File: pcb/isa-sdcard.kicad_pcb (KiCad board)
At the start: 2 copper layers, 151.6 x 82.7 mm, 41 parts, among them J1 SDCARD, J2 Bus_ISA_8bit_AB_Rev0, SW1 ADDR SEL, U1 74HC00, U10 74HC74, U11 74HC08, U12 74HC04, U2 74HCT32, U3 74HCT139, U4 74HC163, U5 74HC00, U6 74HC165, U7 74HC595, U8 74HCT688, U9 74HCT245, X1 16MHz

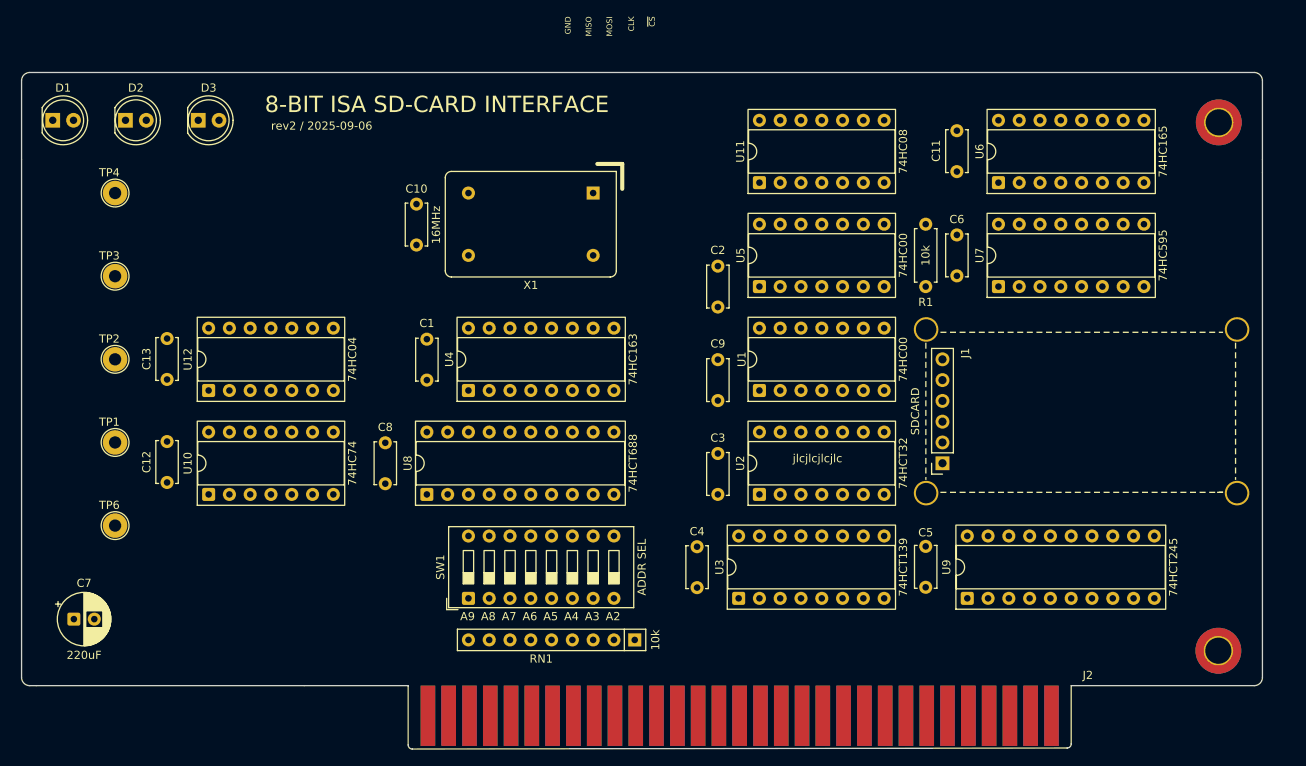
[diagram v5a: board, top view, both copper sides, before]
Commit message: Adding immediate pulse after rwrite and optional pulse after read
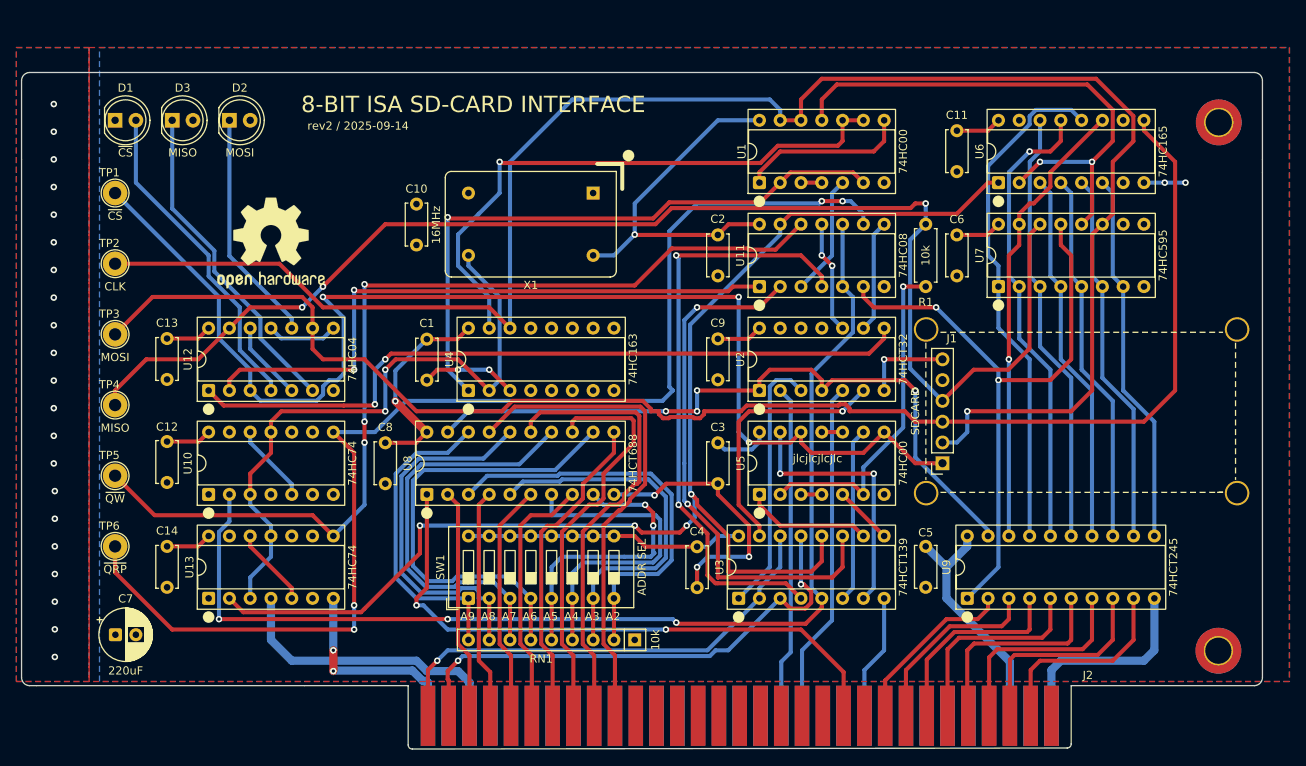
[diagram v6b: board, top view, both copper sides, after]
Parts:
- added C14: 0.1uF, Capacitor_THT:C_Disc_D5.0mm_W2.5mm_P5.00mm, F.Cu at (47.2, 100.5)
- added REF**: OSHW-Logo2_14.6x12mm_SilkScreen, Symbol:OSHW-Logo2_14.6x12mm_SilkScreen, F.Cu at (59.9, 58.4)
- added TP5: ~{QW}, TestPoint:TestPoint_Loop_D2.54mm_Drill1.5mm_Beaded, F.Cu at (40.9, 86.9)
- added U13: 74HC74, Package_DIP:DIP-14_W7.62mm_Socket, F.Cu at (52.3, 101.8)
- D1: value LED -> ~{CS}
- D2: value LED -> MOSI
- D3: value LED -> MISO
- TP6: value ~{Q} -> ~{QRP}
- moved TP1 30.5 mm to (40.9, 52.3)
- moved TP4 25.9 mm to (40.9, 78.2)
- moved U1 25.4 mm to (119.6, 51.0)
- moved U5 25.4 mm to (119.6, 89.1)
- moved U11 12.7 mm to (119.6, 63.7)
- moved U2 12.7 mm to (119.6, 76.4)
- moved D2 12.7 mm to (54.8, 43.4)
- moved TP2 11.7 mm to (40.9, 60.9)
- moved D1 7.62 mm to (40.9, 43.4)
- moved TP3 7.11 mm to (40.9, 69.6)
- moved C7 5.43 mm to (40.9, 106.3)
- moved C11 5.00 mm to (143.7, 49.7), turned to 90 degrees
- moved C2 3.81 mm to (114.5, 62.4)
- moved D3 3.18 mm to (47.9, 43.4)
- moved C9 2.54 mm to (114.5, 75.1)
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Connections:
- U11 pad 1: ~{PULSE} -> Net-(U11-Pad1)
- U11 pad 11: unconnected-(U11-Pad11) -> Net-(U11-Pad11)
- U11 pad 12: GND -> Net-(U13B-~{Q})
- U11 pad 13: GND -> ~{SER_WR}
- U11 pad 2: Net-(U11-Pad2) -> ~{PULSE}
- U12 pad 1: Net-(U11-Pad8) -> Net-(U12-Pad1)
- U12 pad 2: Net-(U11-Pad2) -> Net-(U11-Pad1)
- U2 pad 10: GND -> Net-(U11-Pad11)
- U2 pad 8: unconnected-(U2-Pad8) -> Net-(U12-Pad1)
- U2 pad 9: GND -> Net-(U11-Pad8)
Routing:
- net CLK: track 0.00 -> 216.5 mm, vias 0 -> 1
- net VCC: track 0.00 -> 211.4 mm, vias 0 -> 2
- net MOSI: track 0.00 -> 180.3 mm
- net MISO: track 0.00 -> 165.9 mm, vias 0 -> 3
- net ~{SER_WR}: track 0.00 -> 160.8 mm, vias 0 -> 4
- net ~{CS}: track 0.00 -> 153.0 mm, vias 0 -> 3
- net Net-(U10B-~{Q}): track 0.00 -> 150.8 mm, vias 0 -> 4
- net ~{SER_RD_AND_PULSE}: track 0.00 -> 140.5 mm, vias 0 -> 3
- net GND: track 0.00 -> 127.4 mm, vias 0 -> 31
- net Net-(U13B-~{Q}): track 0.00 -> 118.7 mm, vias 0 -> 3
- net Net-(U12-Pad1): track 0.00 -> 90.5 mm, vias 0 -> 2
- net ~{PORTSEL}: track 0.00 -> 86.8 mm, vias 0 -> 4
- net ~{SER_RD}: track 0.00 -> 78.0 mm, vias 0 -> 2
- net 16MHz: track 0.00 -> 77.7 mm, vias 0 -> 2
- net Net-(U11-Pad1): track 0.00 -> 76.6 mm, vias 0 -> 2
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- added copper zone on B.Cu, net GND
- added copper zone on F.Cu, net GND
- added copper zone on B.Cu, net VCC
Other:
- board text added: "rev2 / 2025-09-14"
- board text removed: "CLK"
- board text removed: "GND"
- board text removed: "MISO"
- board text removed: "MOSI"
- board text removed: "rev2 / 2025-09-06"
- board text removed: "~{CS}"
